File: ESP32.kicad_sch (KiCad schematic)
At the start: 0 parts

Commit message: moved esp32 to heirarchichalca
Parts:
- added C1, C10, C11, C3: 4.7uF, robot-cortex:C_0603_1608Metric, symbol robot-cortex:Capacitor
- added C2, C4, C9: 100nF, robot-cortex:C_0402_1005Metric, symbol robot-cortex:Capacitor
- added Q1, Q2: SS8050-G, robot-cortex:SOT-23-3, symbol robot-cortex:SS8050-G
- added R1, R2, R6: 10k, robot-cortex:R_0402_1005Metric, symbol robot-cortex:Resistor
- added R3: 22k, robot-cortex:R_0402_1005Metric, symbol robot-cortex:Resistor
- added R4: 47.5k, robot-cortex:R_0402_1005Metric, symbol robot-cortex:Resistor
- added R9: 1k, robot-cortex:R_0402_1005Metric, symbol robot-cortex:Resistor
- added U2: ESP32-WROOM-32E-H4, robot-cortex:ESP32-WROOM-32, symbol robot-cortex:ESP32-WROOM-32E-H4
- added U3: DF52-5S-0.8H(21), robot-cortex:DF52-5S-0.8H(21), symbol robot-cortex:DF52-5S-0.8H(21)
- added U4: DF52-4S-0.8H(21), robot-cortex:DF52-4S-0.8H(21), symbol robot-cortex:DF52-4S-0.8H(21)
- added U5: CP2102N-A02-GQFN24R, robot-cortex:QFN50P400X400X80-25N, symbol robot-cortex:CP2102N-A02-GQFN24R
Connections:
- new net: Q2.1 (B), R2.2
- new net: R9.1, U5.9 (~{RST})
- new net: Q1.1 (B), R1.2
- new net 3V3: C1.1, C10.1, C11.1, C2.1, C3.1, C4.1, R6.2, R9.2, U2.2 (3V3), U4.1, U5.5 (VIO), U5.6 (VDD), U5.7 (VREGIN)
- new net CP210x_RX: U2.35 (TXD0), U5.20 (RXD)
- new net CP210x_TX: U2.34 (RXD0), U5.21 (TXD)
- new net CP210x_VBUS: R3.1, R4.2, U5.8 (VBUS)
- new net D+: U5.3 (D+)
- new net D-: U5.4 (D-)
- new net DTR: Q2.2 (E), R1.1, U5.23 (~{DTR})
- new net EN: C9.1, Q1.3 (C), R6.1, U2.3 (EN)
- new net ESP_UART2_RX: U2.27 (IO16), U4.2
- new net ESP_UART2_TX: U2.28 (IO17), U4.3
- new net GND: C1.2, C10.2, C11.2, C2.2, C3.2, C4.2, C9.2, R4.1, U2.1 (GND), U2.15 (GND), U2.38 (GND), U2.39 (P_GND), U3.5, U3.6 (MNT), U3.7 (MNT), U4.4, U4.5 (MNT), U4.6 (MNT), U5.2 (GND), U5.25 (GND__1)
- new net IO0: Q2.3 (C), U2.25 (IO0)
- new net MISO: U2.31 (IO19)
- new net MOSI: U2.37 (IO23)
- new net RTS: Q1.2 (E), R2.1, U5.19 (~{RTS})
- new net SCK: U2.30 (IO18)
- new net SS: U2.29 (IO5)
- new net TCK: U2.16 (IO13/MTCK), U3.4
- new net TDI: U2.14 (IO12/MTDI), U3.3
- new net TDO: U2.23 (IO15/MTDO), U3.1
- new net TMS: U2.13 (IO14/MTMS), U3.2
- new net VUSB: R3.2
- no-connect marks 0 -> 17
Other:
- note added: "Share These Nets Outside Heirarchical Sheet"
- note added: "The uart used by ESP for outside comm"
- note added: "Tying VDD and VREGIN is for when the regulator is not used."

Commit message: commit b4 transition to non-coprocessor. most of sch is done which is good
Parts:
- removed U4: DF52-4S-0.8H(21), robot-cortex:DF52-4S-0.8H(21), symbol robot-cortex:DF52-4S-0.8H(21)
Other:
- moved on the sheet: C1, C2, C3, C4, Q1, Q2, R1, R2, U2, U3

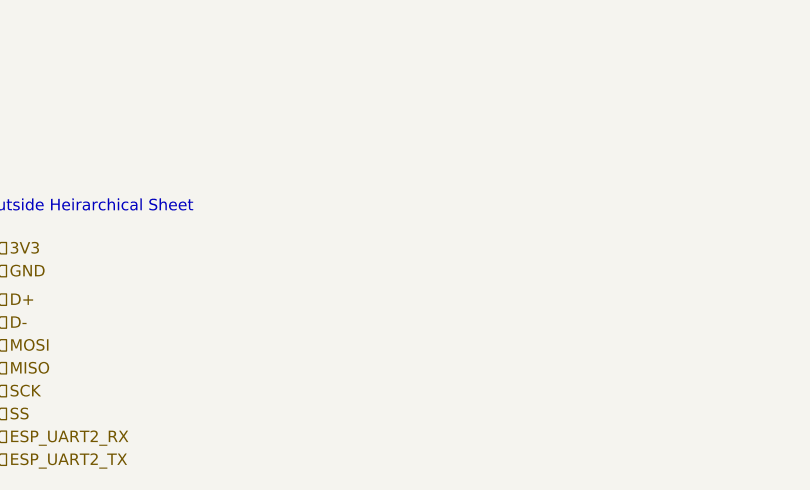
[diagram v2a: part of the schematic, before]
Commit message: heirarchichal sheet label error fix
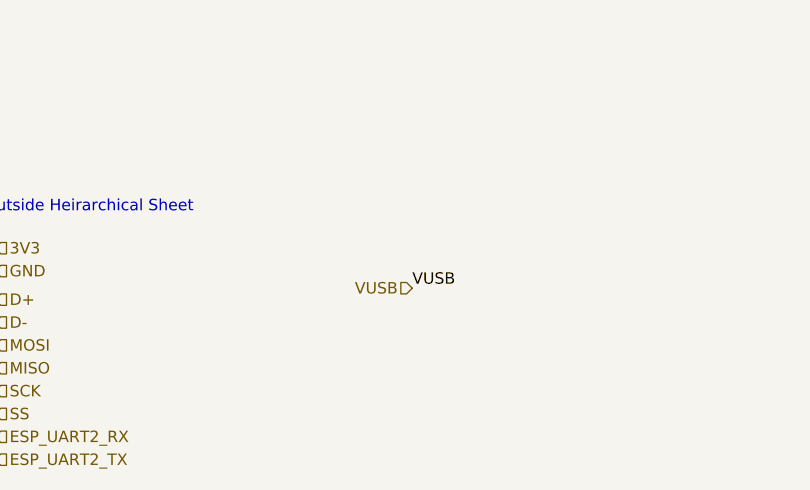
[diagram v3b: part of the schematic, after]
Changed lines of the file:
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@@
     (effects (font (size 1.27 1.27)) (justify right bottom))
+  )
+  (label "VUSB" (at 78.74 171.45 0) (fields_autoplaced)
+    (effects (font (size 1.27 1.27)) (justify left bottom))
   )
   (label "D-" (at 32.385 175.26 180) (fields_autoplaced)
@@
     (effects (font (size 1.27 1.27)) (justify right bottom))
   )
+  (hierarchical_label "VUSB" (shape input) (at 78.74 171.45 180) (fields_autoplaced)
+    (effects (font (size 1.27 1.27)) (justify right))
+  )
   (hierarchical_label "3V3" (shape input) (at 32.385 167.005 0) (fields_autoplaced)

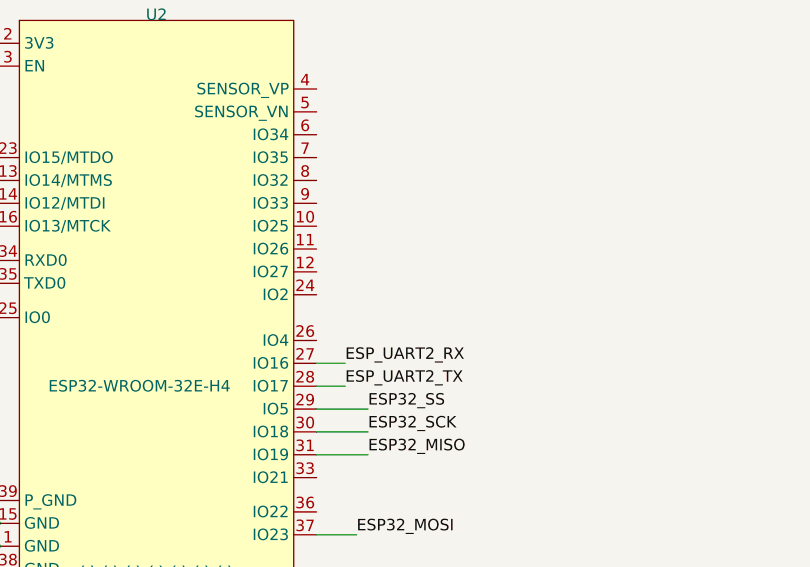
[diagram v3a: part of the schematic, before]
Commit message: sch done sans one additional change, of figuring out how to safely connect VUSB to +5V0 on the CAN transciever
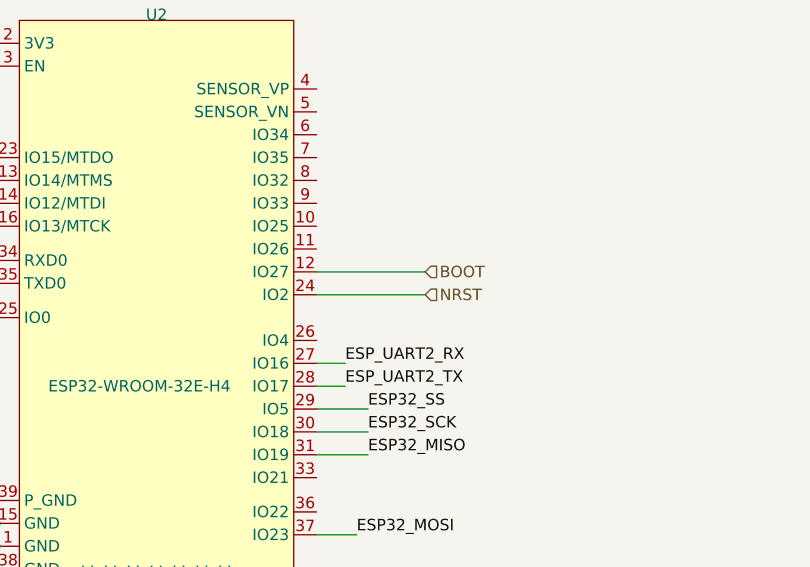
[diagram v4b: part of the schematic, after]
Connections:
- net BOOT: now reaches U2.12 (IO27)
- net NRST: now reaches U2.24 (IO2)
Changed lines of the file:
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@@
+    (stroke (width 0) (type default))
+  )
+  (wire (pts (xy 85.09 88.9) (xy 97.155 88.9))
     (stroke (width 0) (type default))
   )
@@
   )
   (wire (pts (xy 241.3 64.135) (xy 240.03 64.135))
+    (stroke (width 0) (type default))
+  )
+  (wire (pts (xy 85.09 91.44) (xy 97.155 91.44))
     (stroke (width 0) (type default))
   )
@@
     (effects (font (size 1.27 1.27)) (justify left))
   )
+  (hierarchical_label "NRST" (shape input) (at 97.155 91.44 0) (fields_autoplaced)
+    (effects (font (size 1.27 1.27)) (justify left))
+  )
   (hierarchical_label "MISO" (shape input) (at 32.385 180.34 0) (fields_autoplaced)
     (effects (font (size 1.27 1.27)) (justify left))
@@
     (effects (font (size 1.27 1.27)) (justify left))
   )
+  (hierarchical_label "BOOT" (shape input) (at 97.155 88.9 0) (fields_autoplaced)
+    (effects (font (size 1.27 1.27)) (justify left))
+  )

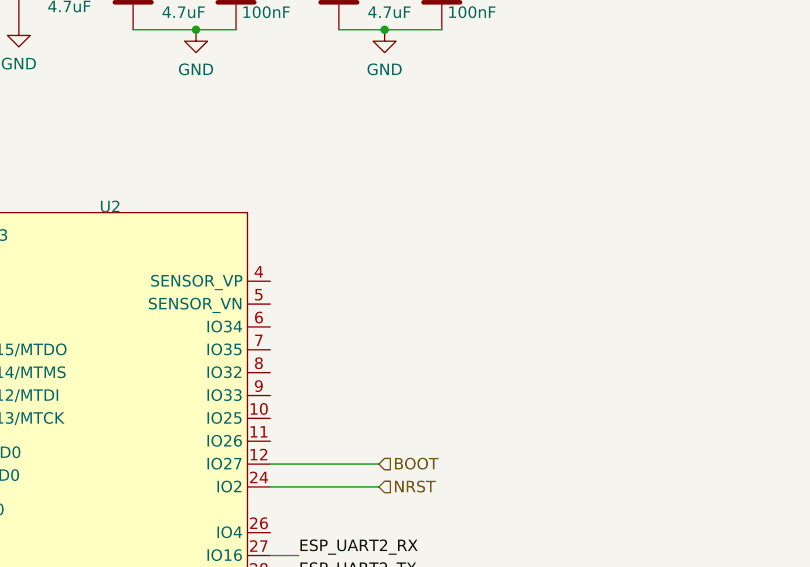
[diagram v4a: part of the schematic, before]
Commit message: updated power supply method
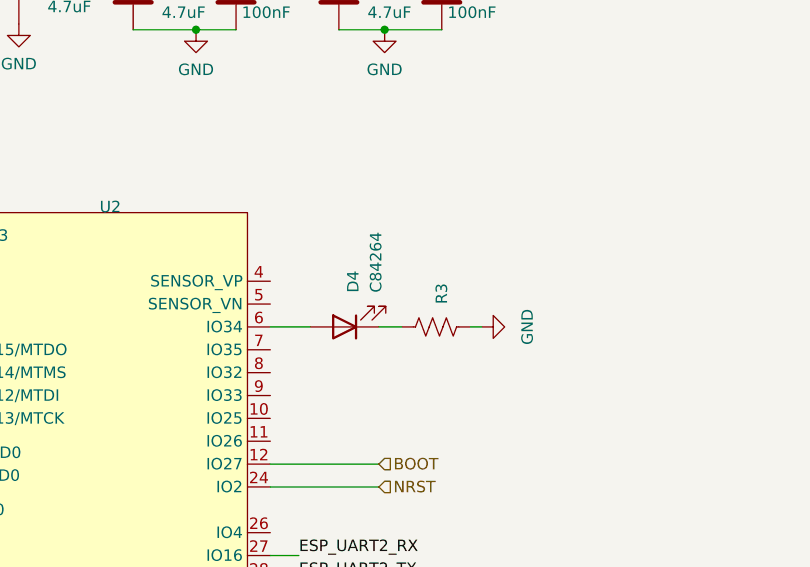
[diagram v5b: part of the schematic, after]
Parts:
- added D4: C84264, robot-cortex:LED_0603_1608Metric, symbol foc-pcb:LED
- added R3: 470, robot-cortex:R_0402_1005Metric, symbol foc-pcb:Resistor
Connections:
- net GND: now also R3.2
- net at U2.6 (IO34): now also D4.2 (A)
- new net: D4.1 (K), R3.1
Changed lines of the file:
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@@
+    (stroke (width 0) (type default))
+  )
+  (wire (pts (xy 97.155 73.66) (xy 99.695 73.66))
     (stroke (width 0) (type default))
   )
@@
     (stroke (width 0) (type default))
   )
+  (wire (pts (xy 108.585 73.66) (xy 107.315 73.66))
+    (stroke (width 0) (type default))
+  )
   (wire (pts (xy 210.185 123.825) (xy 211.455 123.825))
     (stroke (width 0) (type default))
@@
   )
   (wire (pts (xy 97.79 33.02) (xy 104.14 33.02))
+    (stroke (width 0) (type default))
+  )
+  (wire (pts (xy 85.09 73.66) (xy 89.535 73.66))
     (stroke (width 0) (type default))
   )
@@
         )
         (path "/19e4cb9f-d0a4-4ce0-8aa4-5fe95563dc37/f0bc1f65-be22-4560-b9a6-e8d351c4e4ea"
-          (reference "#PWR05") (unit 1)
+          (reference "#PWR039") (unit 1)
         )
       )
@@
         )
         (path "/19e4cb9f-d0a4-4ce0-8aa4-5fe95563dc37/f0bc1f65-be22-4560-b9a6-e8d351c4e4ea"
-          (reference "R4") (unit 1)
+          (reference "R7") (unit 1)
         )
       )
@@
         )
         (path "/19e4cb9f-d0a4-4ce0-8aa4-5fe95563dc37/f0bc1f65-be22-4560-b9a6-e8d351c4e4ea"
-          (reference "C9") (unit 1)
+          (reference "C15") (unit 1)
         )
       )
@@
         )
         (path "/19e4cb9f-d0a4-4ce0-8aa4-5fe95563dc37/f0bc1f65-be22-4560-b9a6-e8d351c4e4ea"
-          (reference "C1") (unit 1)
+          (reference "C20") (unit 1)
         )
       )
@@
         )
         (path "/19e4cb9f-d0a4-4ce0-8aa4-5fe95563dc37/f0bc1f65-be22-4560-b9a6-e8d351c4e4ea"
-          (reference "#PWR021") (unit 1)
+          (reference "#PWR036") (unit 1)
         )
       )
@@
         )
         (path "/19e4cb9f-d0a4-4ce0-8aa4-5fe95563dc37/f0bc1f65-be22-4560-b9a6-e8d351c4e4ea"
-          (reference "C2") (unit 1)
+          (reference "C21") (unit 1)
         )
       )
@@
         )
         (path "/19e4cb9f-d0a4-4ce0-8aa4-5fe95563dc37/f0bc1f65-be22-4560-b9a6-e8d351c4e4ea"
-          (reference "C11") (unit 1)
+          (reference "C17") (unit 1)
         )
       )
@@
         )
         (path "/19e4cb9f-d0a4-4ce0-8aa4-5fe95563dc37/f0bc1f65-be22-4560-b9a6-e8d351c4e4ea"
-          (reference "C3") (unit 1)
+          (reference "C18") (unit 1)
         )
       )
@@
         )
         (path "/19e4cb9f-d0a4-4ce0-8aa4-5fe95563dc37/f0bc1f65-be22-4560-b9a6-e8d351c4e4ea"
-          (reference "#PWR01") (unit 1)
+          (reference "#PWR040") (unit 1)
+        )
+      )
+    )
+  )
+  (symbol (lib_id "foc-pcb:LED") (at 93.345 73.66 180) (unit 1)
+    (in_bom yes) (on_board yes) (dnp no) (fields_autoplaced)
+    (property "Reference" "D4" (at 94.2975 69.85 90)
+      (effects (font (size 1.27 1.27)) (justify right))
+    )
+    (property "Value" "C84264" (at 96.8375 69.85 90)
+      (effects (font (size 1.27 1.27)) (justify right))
+    )
+    (property "Footprint" "robot-cortex:LED_0603_1608Metric" (at 93.345 73.66 0)
+      (effects (font (size 1.27 1.27)) hide)
+    )
+    (property "Datasheet" "~" (at 93.345 73.66 0)
+      (effects (font (size 1.27 1.27)) hide)
+    )
+    (pin "1")
+    (pin "2")
+    (instances
+      (project "robot-cortex"
+        (path "/19e4cb9f-d0a4-4ce0-8aa4-5fe95563dc37"
+          (reference "D4") (unit 1)
+        )
+        (path "/19e4cb9f-d0a4-4ce0-8aa4-5fe95563dc37/f0bc1f65-be22-4560-b9a6-e8d351c4e4ea"
+          (reference "D7") (unit 1)
+        )
+      )
+      (project "foc-pcb"
+        (path "/2b52ab19-a93e-4439-8602-a1380e4825c0"
+          (reference "D1") (unit 1)
         )
       )
@@
         )
         (path "/19e4cb9f-d0a4-4ce0-8aa4-5fe95563dc37/f0bc1f65-be22-4560-b9a6-e8d351c4e4ea"
-          (reference "#PWR07") (unit 1)
+          (reference "#PWR034") (unit 1)
         )
       )
@@
         )
         (path "/19e4cb9f-d0a4-4ce0-8aa4-5fe95563dc37/f0bc1f65-be22-4560-b9a6-e8d351c4e4ea"
-          (reference "R3") (unit 1)
+          (reference "R9") (unit 1)
+        )
+      )
+    )
+  )
+  (symbol (lib_id "power:GND") (at 108.585 73.66 90) (mirror x) (unit 1)
+    (in_bom yes) (on_board yes) (dnp no) (fields_autoplaced)
+    (property "Reference" "#PWR03" (at 114.935 73.66 0)
+      (effects (font (size 1.27 1.27)) hide)
+    )
+    (property "Value" "GND" (at 113.665 73.66 0)
+      (effects (font (size 1.27 1.27)))
+    )
+    (property "Footprint" "" (at 108.585 73.66 0)
+      (effects (font (size 1.27 1.27)) hide)
+    )
+    (property "Datasheet" "" (at 108.585 73.66 0)
+      (effects (font (size 1.27 1.27)) hide)
+    )
+    (pin "1")
+    (instances
+      (project "robot-cortex"
+        (path "/19e4cb9f-d0a4-4ce0-8aa4-5fe95563dc37"
+          (reference "#PWR03") (unit 1)
+        )
+        (path "/19e4cb9f-d0a4-4ce0-8aa4-5fe95563dc37/f0bc1f65-be22-4560-b9a6-e8d351c4e4ea"
+          (reference "#PWR044") (unit 1)
+        )
+      )
+      (project "foc-pcb"
+        (path "/2b52ab19-a93e-4439-8602-a1380e4825c0"
+          (reference "#PWR04") (unit 1)
         )
       )
@@
         )
         (path "/19e4cb9f-d0a4-4ce0-8aa4-5fe95563dc37/f0bc1f65-be22-4560-b9a6-e8d351c4e4ea"
-          (reference "U5") (unit 1)
+          (reference "U9") (unit 1)
         )
       )
@@
         )
         (path "/19e4cb9f-d0a4-4ce0-8aa4-5fe95563dc37/f0bc1f65-be22-4560-b9a6-e8d351c4e4ea"
-          (reference "C10") (unit 1)
+          (reference "C16") (unit 1)
         )
       )
@@
         )
         (path "/19e4cb9f-d0a4-4ce0-8aa4-5fe95563dc37/f0bc1f65-be22-4560-b9a6-e8d351c4e4ea"
-          (reference "R2") (unit 1)
+          (reference "R6") (unit 1)
         )
       )
@@
         )
         (path "/19e4cb9f-d0a4-4ce0-8aa4-5fe95563dc37/f0bc1f65-be22-4560-b9a6-e8d351c4e4ea"
-          (reference "R9") (unit 1)
+          (reference "R8") (unit 1)
         )
       )
@@
         )
         (path "/19e4cb9f-d0a4-4ce0-8aa4-5fe95563dc37/f0bc1f65-be22-4560-b9a6-e8d351c4e4ea"
-          (reference "R6") (unit 1)
+          (reference "R4") (unit 1)
         )
       )
@@
         )
         (path "/19e4cb9f-d0a4-4ce0-8aa4-5fe95563dc37/f0bc1f65-be22-4560-b9a6-e8d351c4e4ea"
-          (reference "#PWR02") (unit 1)
+          (reference "#PWR042") (unit 1)
         )
       )
@@
         )
         (path "/19e4cb9f-d0a4-4ce0-8aa4-5fe95563dc37/f0bc1f65-be22-4560-b9a6-e8d351c4e4ea"
-          (reference "#PWR04") (unit 1)
+          (reference "#PWR037") (unit 1)
         )
       )
@@
         )
         (path "/19e4cb9f-d0a4-4ce0-8aa4-5fe95563dc37/f0bc1f65-be22-4560-b9a6-e8d351c4e4ea"
-          (reference "U2") (unit 1)
+          (reference "U8") (unit 1)
+        )
+      )
+    )
+  )
+  (symbol (lib_id "foc-pcb:Resistor") (at 103.505 73.66 90) (unit 1)
+    (in_bom yes) (on_board yes) (dnp no) (fields_autoplaced)
+    (property "Reference" "R3" (at 104.14 71.12 0)
+      (effects (font (size 1.27 1.27)) (justify left))
+    )
+    (property "Value" "470" (at 103.505 76.2 90)
+      (effects (font (size 1.27 1.27)) hide)
+    )
+    (property "Footprint" "robot-cortex:R_0402_1005Metric" (at 90.805 78.74 0)
+      (effects (font (size 1.27 1.27)) hide)
+    )
+    (property "Datasheet" "~" (at 103.505 73.66 0)
+      (effects (font (size 1.27 1.27)) hide)
+    )
+    (pin "1")
+    (pin "2")
+    (instances
+      (project "robot-cortex"
+        (path "/19e4cb9f-d0a4-4ce0-8aa4-5fe95563dc37"
+          (reference "R3") (unit 1)
+        )
+        (path "/19e4cb9f-d0a4-4ce0-8aa4-5fe95563dc37/f0bc1f65-be22-4560-b9a6-e8d351c4e4ea"
+          (reference "R17") (unit 1)
+        )
+      )
+      (project "foc-pcb"
+        (path "/2b52ab19-a93e-4439-8602-a1380e4825c0"
+          (reference "R4") (unit 1)
         )
       )
@@
         )
         (path "/19e4cb9f-d0a4-4ce0-8aa4-5fe95563dc37/f0bc1f65-be22-4560-b9a6-e8d351c4e4ea"
-          (reference "#PWR014") (unit 1)
+          (reference "#PWR035") (unit 1)
         )
       )
@@
         )
         (path "/19e4cb9f-d0a4-4ce0-8aa4-5fe95563dc37/f0bc1f65-be22-4560-b9a6-e8d351c4e4ea"
-          (reference "R1") (unit 1)
+          (reference "R5") (unit 1)
         )
       )
@@
         )
         (path "/19e4cb9f-d0a4-4ce0-8aa4-5fe95563dc37/f0bc1f65-be22-4560-b9a6-e8d351c4e4ea"
-          (reference "#PWR026") (unit 1)
+          (reference "#PWR041") (unit 1)
         )
       )
@@
         )
         (path "/19e4cb9f-d0a4-4ce0-8aa4-5fe95563dc37/f0bc1f65-be22-4560-b9a6-e8d351c4e4ea"
-          (reference "#PWR020") (unit 1)
+          (reference "#PWR033") (unit 1)
         )
       )
@@
         )
         (path "/19e4cb9f-d0a4-4ce0-8aa4-5fe95563dc37/f0bc1f65-be22-4560-b9a6-e8d351c4e4ea"
-          (reference "U3") (unit 1)
+          (reference "U7") (unit 1)
         )
       )
@@
         )
         (path "/19e4cb9f-d0a4-4ce0-8aa4-5fe95563dc37/f0bc1f65-be22-4560-b9a6-e8d351c4e4ea"
-          (reference "#PWR022") (unit 1)
+          (reference "#PWR038") (unit 1)
         )
       )
@@
         )
         (path "/19e4cb9f-d0a4-4ce0-8aa4-5fe95563dc37/f0bc1f65-be22-4560-b9a6-e8d351c4e4ea"
-          (reference "C4") (unit 1)
+          (reference "C19") (unit 1)
         )
       )
@@
         )
         (path "/19e4cb9f-d0a4-4ce0-8aa4-5fe95563dc37/f0bc1f65-be22-4560-b9a6-e8d351c4e4ea"
-          (reference "#PWR08") (unit 1)
-        )
-      )
+          (reference "#PWR032") (unit 1)
+        )
+      )
